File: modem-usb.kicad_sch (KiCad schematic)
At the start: 5 parts, among them J2 USB4105-GF-A-060, U1 USBLC6-2SC6

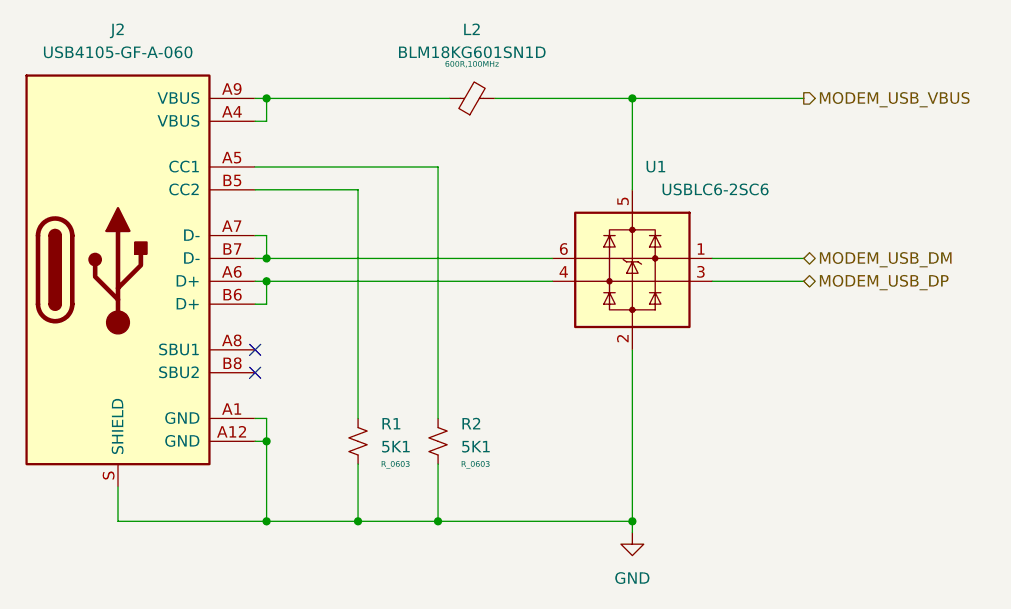
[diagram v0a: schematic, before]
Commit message: Reannotate components
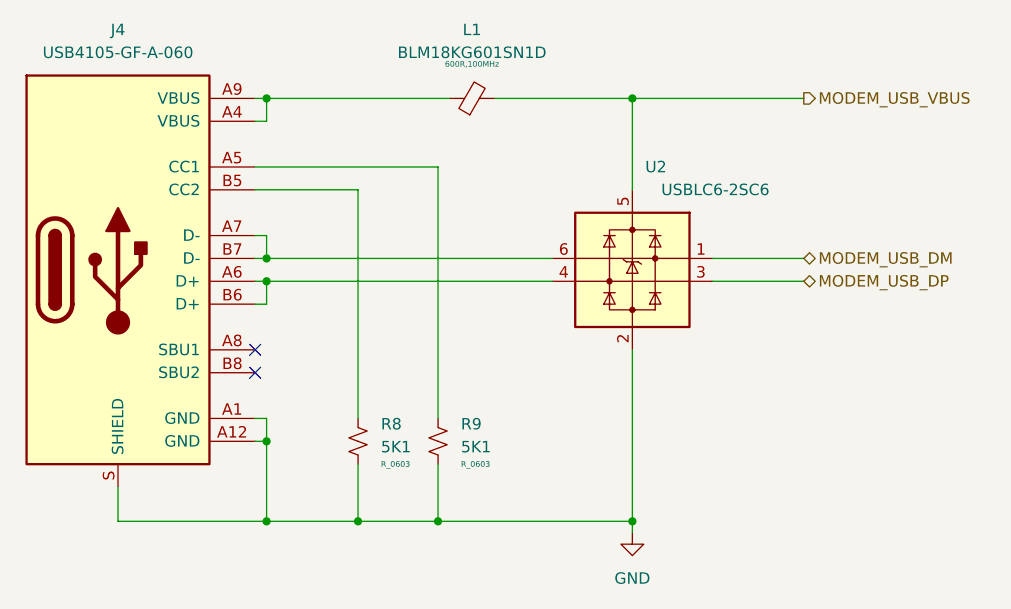
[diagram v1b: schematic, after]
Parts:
- removed J2: USB4105-GF-A-060, J_Connector:USB_C_USB4105-GF-A-060, symbol J_Connector:USB4105-GF-A-060
- removed R1, R2: 5K1, R_Resistor:R_0603, symbol R_Resistor:R_0603
- removed U1: USBLC6-2SC6, U_IC:SOT23_6, symbol U_Basic:USBLC6-2SC6
- added J4: USB4105-GF-A-060, J_Connector:USB_C_USB4105-GF-A-060, symbol J_Connector:USB4105-GF-A-060
- added R8, R9: 5K1, R_Resistor:R_0603, symbol R_Resistor:R_0603
- added U2: USBLC6-2SC6, U_IC:SOT23_6, symbol U_Basic:USBLC6-2SC6
- renumbered L2 to L1
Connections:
- net GND: now also J4.A1 (GND), J4.A12 (GND), J4.S (SHIELD), R8.2, R9.2, U2.2
- net MODEM_USB_DM: now also U2.1
- net MODEM_USB_DP: now also U2.3
- net MODEM_USB_VBUS: now also U2.5
- net at L1.1: now also J4.A4 (VBUS), J4.A9 (VBUS)
- new net: J4.A5 (CC1), R9.1
- new net: J4.A6 (D+), J4.B6 (D+), U2.4
- new net: J4.A7 (D-), J4.B7 (D-), U2.6
- new net: J4.B5 (CC2), R8.1
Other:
- company: (none) -> TL Embedded
- title: (none) -> Winglet Carrier Board
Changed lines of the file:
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@@
 	(generator_version "8.0")
 	(paper "A4")
+	(title_block
+		(title "Winglet Carrier Board")
+		(date "2024-08-09")
+		(rev "v1.0")
+		(company "TL Embedded")
+	)
 	(junction
 		(at 90.17 83.82)
@@
 			)
 			(justify left)
+		)
+	)
+	(symbol
+		(lib_id "power:GND")
+		(at 130.81 114.3 0)
+		(unit 1)
+		(exclude_from_sim no)
+		(in_bom yes)
+		(on_board yes)
+		(dnp no)
+		(fields_autoplaced yes)
+		(property "Reference" "#PWR09"
+			(at 130.81 120.65 0)
+			(effects
+				(font
+					(size 1.27 1.27)
+				)
+				(hide yes)
+			)
+		)
+		(property "Value" "GND"
+			(at 130.81 119.38 0)
+			(effects
+				(font
+					(size 1.27 1.27)
+				)
+			)
+		)
+		(property "Footprint" ""
+			(at 130.81 114.3 0)
+			(effects
+				(font
+					(size 1.27 1.27)
+				)
+				(hide yes)
+			)
+		)
+		(property "Datasheet" ""
+			(at 130.81 114.3 0)
+			(effects
+				(font
+					(size 1.27 1.27)
+				)
+				(hide yes)
+			)
+		)
+		(property "Description" ""
+			(at 130.81 114.3 0)
+			(effects
+				(font
+					(size 1.27 1.27)
+				)
+				(hide yes)
+			)
+		)
+		(pin "1"
+		)
+		(instances
+			(project "Winglet-Carrier"
+				(path "/bbb905ef-a222-43ea-83e2-d1132f7d94bb/b1159f78-859e-4998-9001-fd5ae922e822"
+					(reference "#PWR09")
+					(unit 1)
+				)
+			)
+		)
+	)
+	(symbol
+		(lib_id "R_Resistor:R_0603")
+		(at 109.22 104.14 0)
+		(unit 1)
+		(exclude_from_sim no)
+		(in_bom yes)
+		(on_board yes)
+		(dnp no)
+		(property "Reference" "R9"
+			(at 111.76 102.235 0)
+			(effects
+				(font
+					(size 1.27 1.27)
+				)
+				(justify left)
+			)
+		)
+		(property "Value" "5K1"
+			(at 111.76 104.775 0)
+			(effects
+				(font
+					(size 1.27 1.27)
+				)
+				(justify left)
+			)
+		)
+		(property "Footprint" "R_Resistor:R_0603"
+			(at 106.68 104.14 90)
+			(effects
+				(font
+					(size 1.27 1.27)
+				)
+				(hide yes)
+			)
+		)
+		(property "Datasheet" ""
+			(at 106.68 107.95 0)
+			(effects
+				(font
+					(size 1.27 1.27)
+				)
+				(hide yes)
+			)
+		)
+		(property "Description" ""
+			(at 109.22 104.14 0)
+			(effects
+				(font
+					(size 1.27 1.27)
+				)
+				(hide yes)
+			)
+		)
+		(property "Size" "R_0603"
+			(at 111.76 106.68 0)
+			(effects
+				(font
+					(size 0.635 0.635)
+				)
+				(justify left)
+			)
+		)
+		(pin "1"
+		)
+		(pin "2"
+		)
+		(instances
+			(project "Winglet-Carrier"
+				(path "/bbb905ef-a222-43ea-83e2-d1132f7d94bb/b1159f78-859e-4998-9001-fd5ae922e822"
+					(reference "R9")
+					(unit 1)
+				)
+			)
 		)
 	)
@@
 		(dnp no)
 		(fields_autoplaced yes)
-		(property "Reference" "J2"
+		(property "Reference" "J4"
 			(at 73.66 58.42 0)
 			(effects
@@
 			(project "Winglet-Carrier"
 				(path "/bbb905ef-a222-43ea-83e2-d1132f7d94bb/b1159f78-859e-4998-9001-fd5ae922e822"
-					(reference "J2")
+					(reference "J4")
 					(unit 1)
 				)
@@
 	)
 	(symbol
-		(lib_id "power:GND")
-		(at 130.81 114.3 0)
+		(lib_id "R_Resistor:R_0603")
+		(at 100.33 104.14 0)
 		(unit 1)
 		(exclude_from_sim no)
@@
 		(dnp no)
 		(fields_autoplaced yes)
-		(property "Reference" "#PWR07"
-			(at 130.81 120.65 0)
-			(effects
-				(font
-					(size 1.27 1.27)
-				)
-				(hide yes)
-			)
-		)
-		(property "Value" "GND"
-			(at 130.81 119.38 0)
-			(effects
-				(font
-					(size 1.27 1.27)
-				)
-			)
-		)
-		(property "Footprint" ""
-			(at 130.81 114.3 0)
+		(property "Reference" "R8"
+			(at 102.87 102.235 0)
+			(effects
+				(font
+					(size 1.27 1.27)
+				)
+				(justify left)
+			)
+		)
+		(property "Value" "5K1"
+			(at 102.87 104.775 0)
+			(effects
+				(font
+					(size 1.27 1.27)
+				)
+				(justify left)
+			)
+		)
+		(property "Footprint" "R_Resistor:R_0603"
+			(at 97.79 104.14 90)
 			(effects
 				(font
@@
 		)
 		(property "Datasheet" ""
-			(at 130.81 114.3 0)
+			(at 97.79 107.95 0)
 			(effects
 				(font
@@
 		)
 		(property "Description" ""
-			(at 130.81 114.3 0)
-			(effects
-				(font
-					(size 1.27 1.27)
-				)
-				(hide yes)
+			(at 100.33 104.14 0)
+			(effects
+				(font
+					(size 1.27 1.27)
+				)
+				(hide yes)
+			)
+		)
+		(property "Size" "R_0603"
+			(at 102.87 106.68 0)
+			(effects
+				(font
+					(size 0.635 0.635)
+				)
+				(justify left)
 			)
 		)
 		(pin "1"
+		)
+		(pin "2"
 		)
 		(instances
 			(project "Winglet-Carrier"
 				(path "/bbb905ef-a222-43ea-83e2-d1132f7d94bb/b1159f78-859e-4998-9001-fd5ae922e822"
-					(reference "#PWR07")
+					(reference "R8")
 					(unit 1)
 				)
@@
 		(on_board yes)
 		(dnp no)
-		(property "Reference" "U1"
+		(property "Reference" "U2"
 			(at 134.62 73.66 0)
 			(effects
@@
 			(project "Winglet-Carrier"
 				(path "/bbb905ef-a222-43ea-83e2-d1132f7d94bb/b1159f78-859e-4998-9001-fd5ae922e822"
-					(reference "U1")
-					(unit 1)
-				)
-			)
-		)
-	)
-	(symbol
-		(lib_id "R_Resistor:R_0603")
-		(at 109.22 104.14 0)
-		(unit 1)
-		(exclude_from_sim no)
-		(in_bom yes)
-		(on_board yes)
-		(dnp no)
-		(property "Reference" "R2"
-			(at 111.76 102.235 0)
-			(effects
-				(font
-					(size 1.27 1.27)
-				)
-				(justify left)
-			)
-		)
-		(property "Value" "5K1"
-			(at 111.76 104.775 0)
-			(effects
-				(font
-					(size 1.27 1.27)
-				)
-				(justify left)
-			)
-		)
-		(property "Footprint" "R_Resistor:R_0603"
-			(at 106.68 104.14 90)
-			(effects
-				(font
-					(size 1.27 1.27)
-				)
-				(hide yes)
-			)
-		)
-		(property "Datasheet" ""
-			(at 106.68 107.95 0)
-			(effects
-				(font
-					(size 1.27 1.27)
-				)
-				(hide yes)
-			)
-		)
-		(property "Description" ""
-			(at 109.22 104.14 0)
-			(effects
-				(font
-					(size 1.27 1.27)
-				)
-				(hide yes)
-			)
-		)
-		(property "Size" "R_0603"
-			(at 111.76 106.68 0)
-			(effects
-				(font
-					(size 0.635 0.635)
-				)
-				(justify left)
-			)
-		)
-		(pin "1"
-		)
-		(pin "2"
-		)
-		(instances
-			(project "Winglet-Carrier"
-				(path "/bbb905ef-a222-43ea-83e2-d1132f7d94bb/b1159f78-859e-4998-9001-fd5ae922e822"
-					(reference "R2")
+					(reference "U2")
 					(unit 1)
 				)
@@
 		(dnp no)
 		(fields_autoplaced yes)
-		(property "Reference" "L2"
+		(property "Reference" "L1"
 			(at 112.9919 58.42 90)
 			(effects
@@
 			(project "Winglet-Carrier"
 				(path "/bbb905ef-a222-43ea-83e2-d1132f7d94bb/b1159f78-859e-4998-9001-fd5ae922e822"
-					(reference "L2")
+					(reference "L1")
 					(unit 1)
 				)
-			)
-		)
-	)
-	(symbol
-		(lib_id "R_Resistor:R_0603")
-		(at 100.33 104.14 0)
-		(unit 1)
-		(exclude_from_sim no)
-		(in_bom yes)
-		(on_board yes)
-		(dnp no)
-		(fields_autoplaced yes)
-		(property "Reference" "R1"
-			(at 102.87 102.235 0)
-			(effects
-				(font
-					(size 1.27 1.27)
-				)
-				(justify left)
-			)
-		)
-		(property "Value" "5K1"
-			(at 102.87 104.775 0)
-			(effects
-				(font
-					(size 1.27 1.27)
-				)
-				(justify left)
-			)
-		)
-		(property "Footprint" "R_Resistor:R_0603"
-			(at 97.79 104.14 90)
-			(effects
-				(font
-					(size 1.27 1.27)
-				)
-				(hide yes)
-			)
-		)
-		(property "Datasheet" ""
-			(at 97.79 107.95 0)
-			(effects
-				(font
-					(size 1.27 1.27)
-				)
-				(hide yes)
-			)
-		)
-		(property "Description" ""
-			(at 100.33 104.14 0)
-			(effects
-				(font
-					(size 1.27 1.27)
-				)
-				(hide yes)
-			)
-		)
-		(property "Size" "R_0603"
-			(at 102.87 106.68 0)
-			(effects
-				(font
-					(size 0.635 0.635)
-				)
-				(justify left)
-			)
-		)
-		(pin "1"
-		)
-		(pin "2"
-		)
-		(instances
-			(project "Winglet-Carrier"
-				(path "/bbb905ef-a222-43ea-83e2-d1132f7d94bb/b1159f78-859e-4998-9001-fd5ae922e822"
-					(reference "R1")
-					(unit 1)
-				)
